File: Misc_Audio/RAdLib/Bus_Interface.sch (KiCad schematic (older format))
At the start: 14 parts, among them J1 Raspberry_Pi_2_3, J2 UART_Header, J3 Power_Output_Header, J4 I2C_Header, U101 74AHCT04, U201 74LVC245A, U202 74HCT245, U203 74AHCT125, U204 M24C01-FDW

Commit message: Checkpoint ... board is close to being done.  Still need to tweak the ground plane.
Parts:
- removed JP1: Jumper_3_Bridged12, Connector_PinHeader_2.54mm:PinHeader_1x03_P2.54mm_Vertical, symbol Jumper:Jumper_3_Bridged12
- added C201, C202, C203, C204: .1uF, Capacitor_THT:C_Disc_D5.0mm_W2.5mm_P2.50mm, symbol Device:C_Small
- added JP1: Jumper_2_Open, Connector_PinHeader_2.54mm:PinHeader_1x02_P2.54mm_Vertical, symbol Jumper:Jumper_2_Open
- added R205: 1K, Resistor_THT:R_Axial_DIN0204_L3.6mm_D1.6mm_P5.08mm_Horizontal, symbol Device:R
- J2, J3: footprint Connector_PinHeader_2.54mm:PinHeader_1x03_P2.54mm_Horizontal -> Connector_PinHeader_2.54mm:PinHeader_1x03_P2.54mm_Vertical
- J4: footprint Connector_PinHeader_2.54mm:PinHeader_1x02_P2.54mm_Horizontal -> Connector_PinHeader_2.54mm:PinHeader_1x02_P2.54mm_Vertical
- U203: footprint Package_DIP:DIP-20_W7.62mm -> Package_DIP:DIP-14_W7.62mm
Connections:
- wire segments 75 -> 77

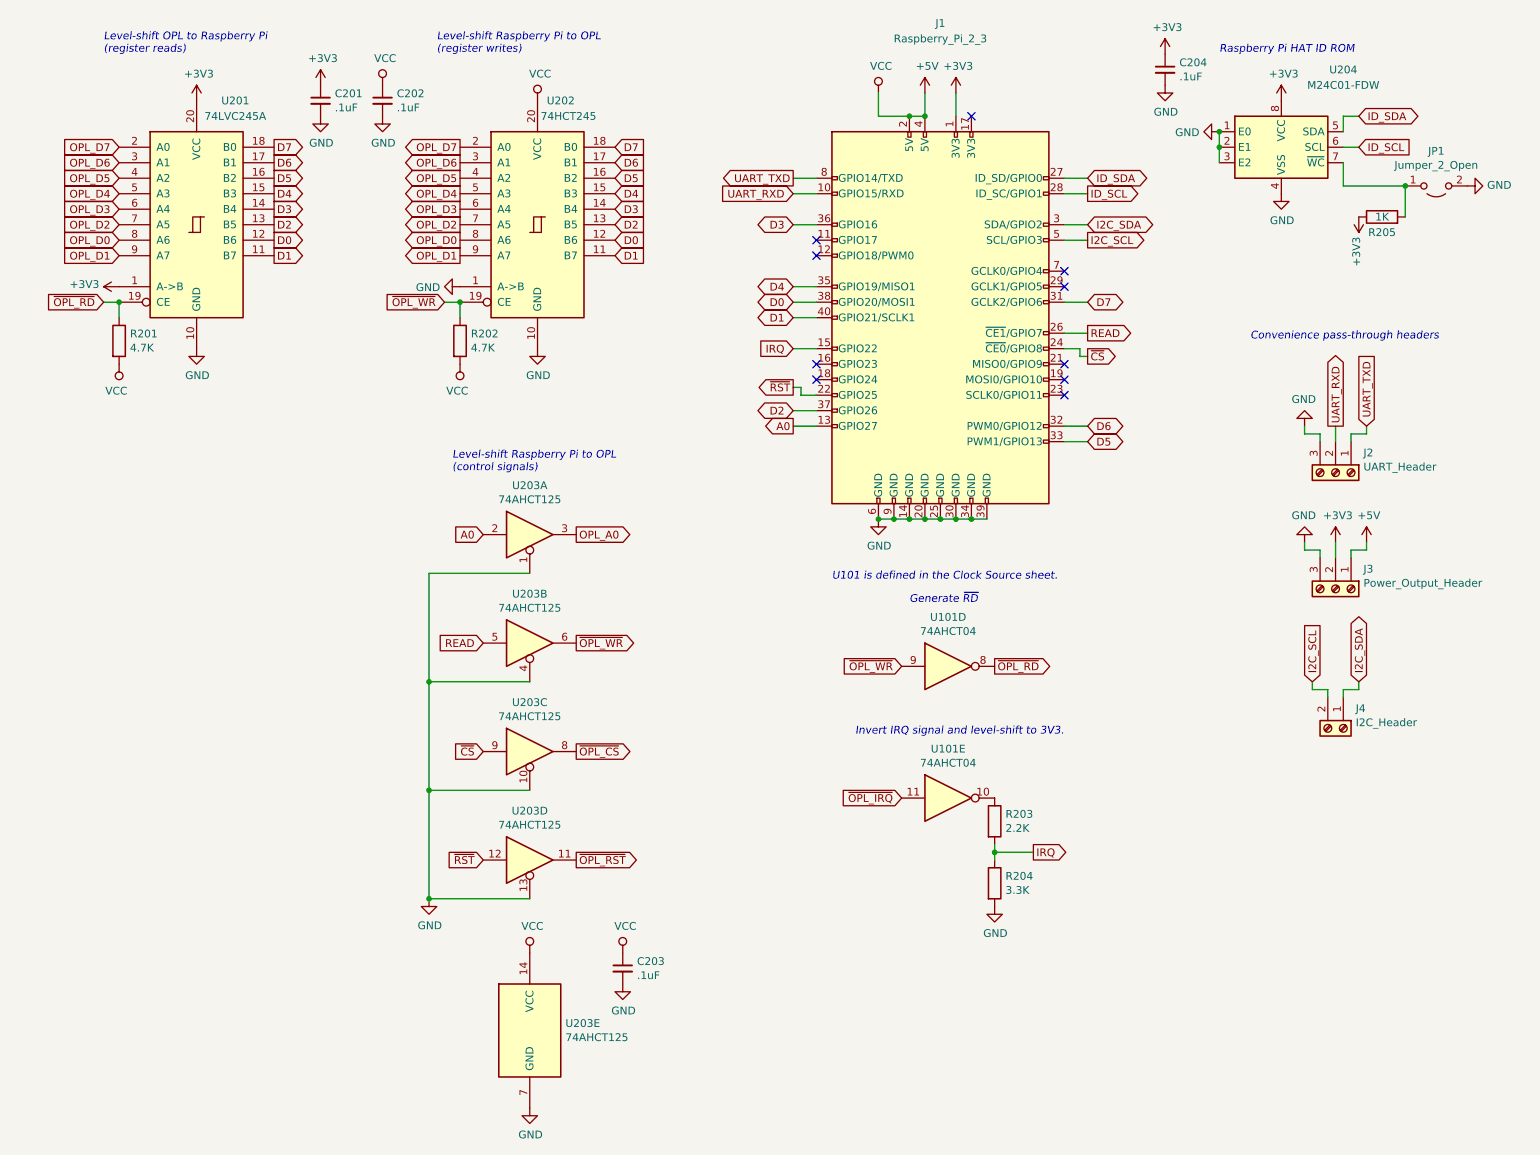
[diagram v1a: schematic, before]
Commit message: Rework the clock to use a self-contained oscillator package.  Remove dependencies on the 7404 in the bus interface.
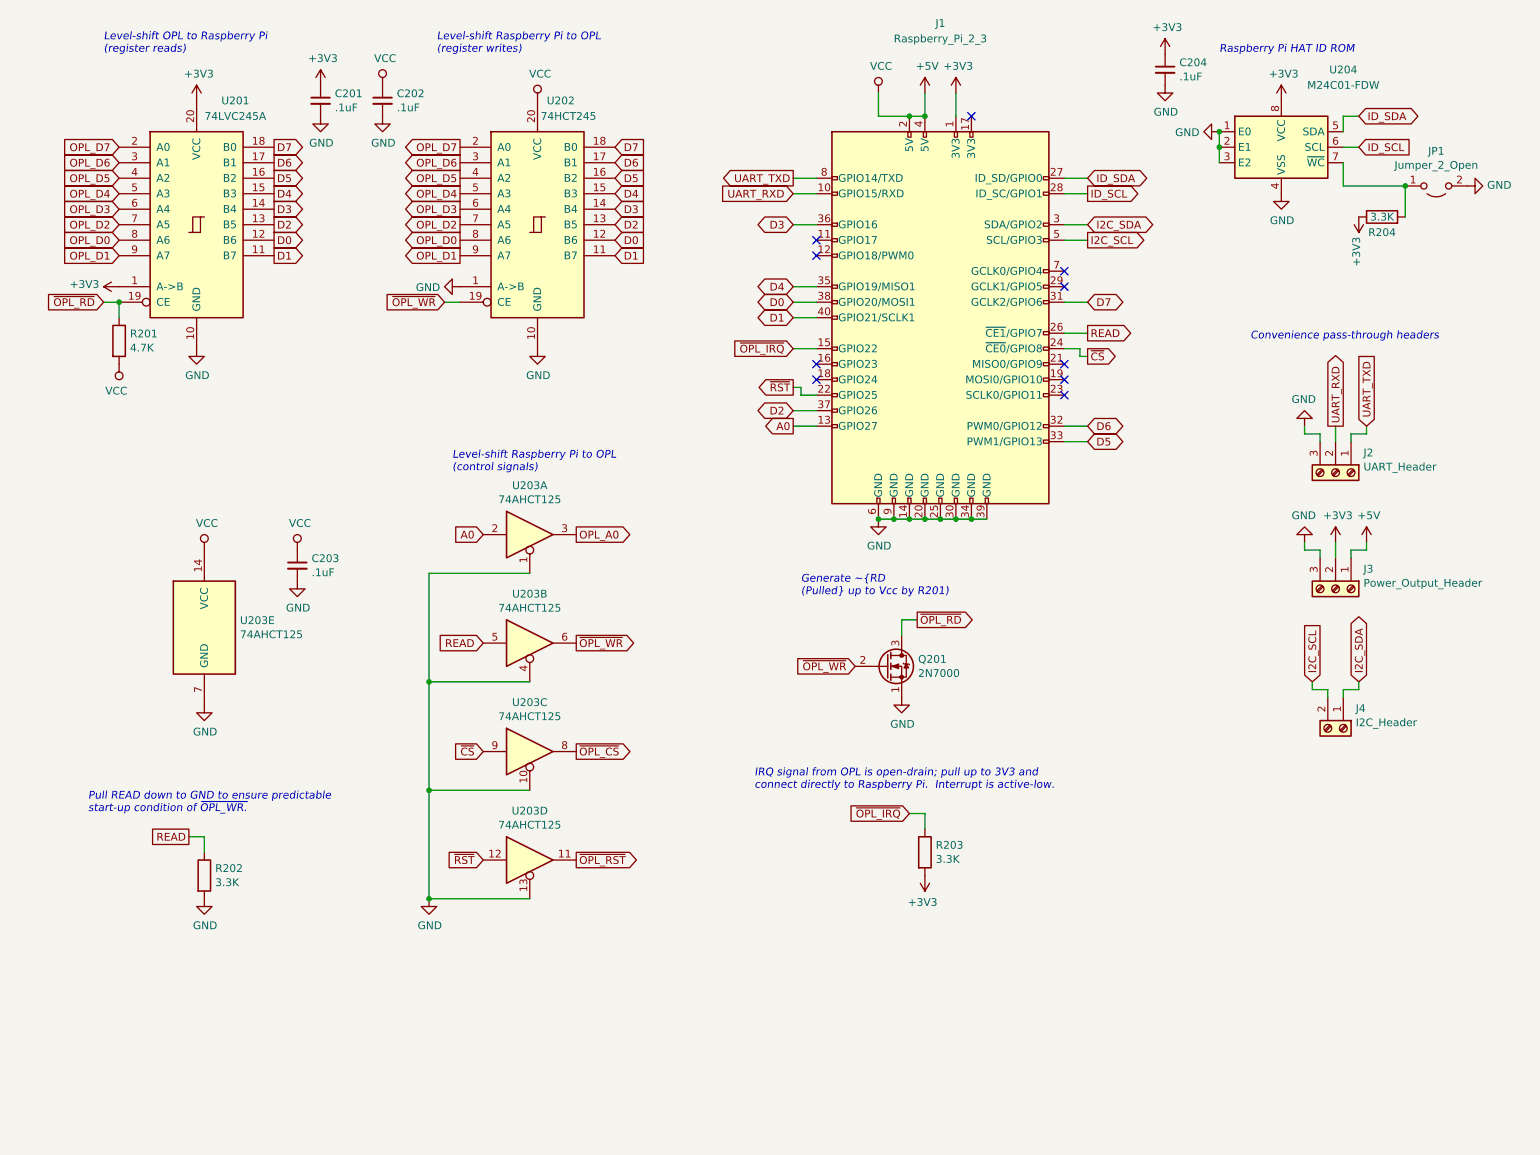
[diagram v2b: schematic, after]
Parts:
- removed R204: 3.3K, Resistor_THT:R_Axial_DIN0204_L3.6mm_D1.6mm_P5.08mm_Horizontal, symbol Device:R
- removed U101: 74AHCT04, Package_DIP:DIP-14_W7.62mm, symbol 74xx:74HC04
- added Q201: 2N7000, Package_TO_SOT_THT:TO-92_HandSolder, symbol Transistor_FET:2N7000
- R202: value 4.7K -> 3.3K; Part Xicon 270-4.7K/REEL-RC -> Xicon 270-3.3K/REEL-RC
- R203: value 2.2K -> 3.3K; Part Xicon 270-2.2K/REEL-RC -> Xicon 270-3.3K/REEL-RC
- R204: renamed from R205; value 1K -> 3.3K
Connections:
- net +3V3: now also R203.2
- net +5V: no longer R202.2
- net GND: now also R202.2, Q201.1 (S)
- net READ: now also R202.1
- net ~OPL_IRQ: now also J1.15 (GPIO22), R203.1
- net ~OPL_RD: now also Q201.3 (D)
- net ~OPL_WR: now also Q201.2 (G); no longer R202.1
- removed net IRQ: J1.15 (GPIO22), R203.2
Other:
- note added: "Generate ~RD\n(Pulled up to Vcc by R201)"
- note added: "IRQ signal from OPL is open-drain; pull up to 3V3 and\nconnect directly to Raspberry Pi. Interrupt is active-low."
- note added: "Pull READ down to GND to ensure predictable\nstart-up condition of ~OPL_WR."
- note removed: "Generate ~RD"
- note removed: "Invert IRQ signal and level-shift to 3V3."
- note removed: "U101 is defined in the Clock Source sheet."
- moved on the sheet: C203, R202, R203, U203E
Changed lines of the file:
@@
 $Descr USLetter 11000 8500
 encoding utf-8
-Sheet 3 3
+Sheet 2 2
 Title "RAdLib - AdLib clone for Raspberry Pi"
 Date "2019-10-10"
@@
 Text GLabel 7300 2750 2    50   Output ~ 0
 READ
-$Comp
-L 74xx:74HC04 U101
-U 4 1 5DA5D1AF
-P 6400 4900
-F 0 "U101" H 6400 5217 50  0000 C CNN
-F 1 "74AHCT04" H 6400 5126 50  0000 C CNN
-F 2 "Package_DIP:DIP-14_W7.62mm" H 6400 4900 50  0001 C CNN
-F 3 "https://assets.nexperia.com/documents/data-sheet/74HC_HCT04.pdf" H 6400 4900 50  0001 C CNN
-	4    6400 4900
-	1    0    0    -1
-$EndComp
-Text GLabel 6100 4900 0    50   Input ~ 0
+Text GLabel 5800 4900 0    50   Input ~ 0
 ~OPL_WR
-Text GLabel 6700 4900 2    50   Output ~ 0
+Text GLabel 6200 4600 2    50   Output ~ 0
 ~OPL_RD
 Wire Wire Line
@@
 	7150 2750 7300 2750
 Text GLabel 5400 2850 0    50   Input ~ 0
-IRQ
+~OPL_IRQ
 NoConn ~ 7150 3050
 NoConn ~ 7150 2950
@@
 L Device:R R202
 U 1 1 5DCAA178
-P 3250 2800
-F 0 "R202" H 3320 2846 50  0000 L CNN
-F 1 "4.7K" H 3320 2755 50  0000 L CNN
-F 2 "Resistor_THT:R_Axial_DIN0204_L3.6mm_D1.6mm_P5.08mm_Horizontal" V 3180 2800 50  0001 C CNN
-F 3 "~" H 3250 2800 50  0001 C CNN
-F 4 "Xicon 270-4.7K/REEL-RC" H 3250 2800 50  0001 C CNN "Part"
-	1    3250 2800
+P 1600 6250
+F 0 "R202" H 1670 6296 50  0000 L CNN
+F 1 "3.3K" H 1670 6205 50  0000 L CNN
+F 2 "Resistor_THT:R_Axial_DIN0204_L3.6mm_D1.6mm_P5.08mm_Horizontal" V 1530 6250 50  0001 C CNN
+F 3 "~" H 1600 6250 50  0001 C CNN
+F 4 "Xicon 270-3.3K/REEL-RC" H 1600 6250 50  0001 C CNN "Part"
+	1    1600 6250
 	1    0    0    -1
 $EndComp
@@
 Wire Wire Line
 	3150 2550 3250 2550
-Wire Wire Line
-	3250 2650 3250 2550
-Connection ~ 3250 2550
-$Comp
-L power:VCC #PWR0135
-U 1 1 5DCB12D8
-P 3250 2950
-F 0 "#PWR0135" H 3250 2800 50  0001 C CNN
-F 1 "VCC" H 3268 3123 50  0000 C CNN
-F 2 "" H 3250 2950 50  0001 C CNN
-F 3 "" H 3250 2950 50  0001 C CNN
-	1    3250 2950
-	-1   0    0    1
-$EndComp
 $Comp
 L 74xx:74LS125 U203
 U 5 1 5DCCCFE6
-P 3700 7250
-F 0 "U203" H 3930 7296 50  0000 L CNN
-F 1 "74AHCT125" H 3930 7205 50  0000 L CNN
-F 2 "Package_DIP:DIP-14_W7.62mm" H 3700 7250 50  0001 C CNN
-F 3 "http://www.ti.com/lit/gpn/sn74LS125" H 3700 7250 50  0001 C CNN
-	5    3700 7250
+P 1600 4650
+F 0 "U203" H 1830 4696 50  0000 L CNN
+F 1 "74AHCT125" H 1830 4605 50  0000 L CNN
+F 2 "Package_DIP:DIP-14_W7.62mm" H 1600 4650 50  0001 C CNN
+F 3 "http://www.ti.com/lit/gpn/sn74LS125" H 1600 4650 50  0001 C CNN
+	5    1600 4650
 	1    0    0    -1
 $EndComp
@@
 L power:VCC #PWR0136
 U 1 1 5DCD0443
-P 3700 6750
-F 0 "#PWR0136" H 3700 6600 50  0001 C CNN
-F 1 "VCC" H 3717 6923 50  0000 C CNN
-F 2 "" H 3700 6750 50  0001 C CNN
-F 3 "" H 3700 6750 50  0001 C CNN
-	1    3700 6750
+P 1600 4150
+F 0 "#PWR0136" H 1600 4000 50  0001 C CNN
+F 1 "VCC" H 1617 4323 50  0000 C CNN
+F 2 "" H 1600 4150 50  0001 C CNN
+F 3 "" H 1600 4150 50  0001 C CNN
+	1    1600 4150
 	1    0    0    -1
 $EndComp
@@
 L power:GND #PWR0137
 U 1 1 5DCD09A2
-P 3700 7750
-F 0 "#PWR0137" H 3700 7500 50  0001 C CNN
-F 1 "GND" H 3705 7577 50  0000 C CNN
-F 2 "" H 3700 7750 50  0001 C CNN
-F 3 "" H 3700 7750 50  0001 C CNN
-	1    3700 7750
+P 1600 5150
+F 0 "#PWR0137" H 1600 4900 50  0001 C CNN
+F 1 "GND" H 1605 4977 50  0000 C CNN
+F 2 "" H 1600 5150 50  0001 C CNN
+F 3 "" H 1600 5150 50  0001 C CNN
+	1    1600 5150
 	1    0    0    -1
 $EndComp
@@
 $EndComp
 Connection ~ 3050 6400
-Text GLabel 6100 5750 0    50   Input ~ 0
+Text GLabel 6150 5850 0    50   Input ~ 0
 ~OPL_IRQ
-$Comp
-L 74xx:74HC04 U101
-U 5 1 5DCDD39D
-P 6400 5750
-F 0 "U101" H 6400 6067 50  0000 C CNN
-F 1 "74AHCT04" H 6400 5976 50  0000 C CNN
-F 2 "Package_DIP:DIP-14_W7.62mm" H 6400 5750 50  0001 C CNN
-F 3 "https://assets.nexperia.com/documents/data-sheet/74HC_HCT04.pdf" H 6400 5750 50  0001 C CNN
-	5    6400 5750
-	1    0    0    -1
-$EndComp
 $Comp
 L Device:R R203
 U 1 1 5DCDEB3B
-P 6700 5900
-F 0 "R203" H 6770 5946 50  0000 L CNN
-F 1 "2.2K" H 6770 5855 50  0000 L CNN
-F 2 "Resistor_THT:R_Axial_DIN0204_L3.6mm_D1.6mm_P5.08mm_Horizontal" V 6630 5900 50  0001 C CNN
-F 3 "~" H 6700 5900 50  0001 C CNN
-F 4 "Xicon 270-2.2K/REEL-RC" H 6700 5900 50  0001 C CNN "Part"
-	1    6700 5900
-	1    0    0    -1
-$EndComp
-$Comp
-L Device:R R204
-U 1 1 5DCDF804
-P 6700 6300
-F 0 "R204" H 6770 6346 50  0000 L CNN
-F 1 "3.3K" H 6770 6255 50  0000 L CNN
-F 2 "Resistor_THT:R_Axial_DIN0204_L3.6mm_D1.6mm_P5.08mm_Horizontal" V 6630 6300 50  0001 C CNN
-F 3 "~" H 6700 6300 50  0001 C CNN
-F 4 "Xicon 270-3.3K-RC" H 6700 6300 50  0001 C CNN "Part"
-	1    6700 6300
-	1    0    0    -1
-$EndComp
-$Comp
-L power:GND #PWR0139
-U 1 1 5DCE303F
-P 6700 6450
-F 0 "#PWR0139" H 6700 6200 50  0001 C CNN
-F 1 "GND" H 6705 6277 50  0000 C CNN
-F 2 "" H 6700 6450 50  0001 C CNN
-F 3 "" H 6700 6450 50  0001 C CNN
-	1    6700 6450
-	1    0    0    -1
-$EndComp
-Wire Wire Line
-	6700 6050 6700 6100
-Text GLabel 6950 6100 2    50   Output ~ 0
-IRQ
-Wire Wire Line
-	6700 6100 6950 6100
-Connection ~ 6700 6100
-Wire Wire Line
-	6700 6100 6700 6150
-Text Notes 5800 5350 0    50   Italic 0
-Invert IRQ signal and level-shift to 3V3.
+P 6250 6100
+F 0 "R203" H 6320 6146 50  0000 L CNN
+F 1 "3.3K" H 6320 6055 50  0000 L CNN
+F 2 "Resistor_THT:R_Axial_DIN0204_L3.6mm_D1.6mm_P5.08mm_Horizontal" V 6180 6100 50  0001 C CNN
+F 3 "~" H 6250 6100 50  0001 C CNN
+F 4 "Xicon 270-3.3K/REEL-RC" H 6250 6100 50  0001 C CNN "Part"
+	1    6250 6100
+	1    0    0    -1
+$EndComp
 Text Notes 3200 3650 0    50   Italic 0
 Level-shift Raspberry Pi to OPL\n(control signals)
-Text Notes 6150 4500 0    50   Italic 0
-Generate ~RD
+Text Notes 5450 4450 0    50   Italic 0
+Generate ~RD\n(Pulled up to Vcc by R201)
 Text Notes 8150 950  0    50   Italic 0
 Raspberry Pi HAT ID ROM
 Text Notes 8350 2800 0    50   Italic 0
 Convenience pass-through headers
-Text Notes 5650 4350 0    50   Italic 0
-U101 is defined in the Clock Source sheet.
 NoConn ~ 5550 2150
 Wire Wire Line
@@
 L Device:C_Small C203
 U 1 1 5DA58D30
-P 4300 6850
-F 0 "C203" H 4392 6896 50  0000 L CNN
-F 1 ".1uF" H 4392 6805 50  0000 L CNN
-F 2 "Capacitor_THT:C_Disc_D5.0mm_W2.5mm_P2.50mm" H 4300 6850 50  0001 C CNN
-F 3 "~" H 4300 6850 50  0001 C CNN
-	1    4300 6850
+P 2200 4250
+F 0 "C203" H 2292 4296 50  0000 L CNN
+F 1 ".1uF" H 2292 4205 50  0000 L CNN
+F 2 "Capacitor_THT:C_Disc_D5.0mm_W2.5mm_P2.50mm" H 2200 4250 50  0001 C CNN
+F 3 "~" H 2200 4250 50  0001 C CNN
+	1    2200 4250
 	1    0    0    -1
 $EndComp
@@
 L power:GND #PWR0152
 U 1 1 5DA6179C
-P 4300 6950
-F 0 "#PWR0152" H 4300 6700 50  0001 C CNN
-F 1 "GND" H 4305 6777 50  0000 C CNN
-F 2 "" H 4300 6950 50  0001 C CNN
-F 3 "" H 4300 6950 50  0001 C CNN
-	1    4300 6950
+P 2200 4350
+F 0 "#PWR0152" H 2200 4100 50  0001 C CNN
+F 1 "GND" H 2205 4177 50  0000 C CNN
+F 2 "" H 2200 4350 50  0001 C CNN
+F 3 "" H 2200 4350 50  0001 C CNN
+	1    2200 4350
 	1    0    0    -1
 $EndComp
@@
 L power:VCC #PWR0153
 U 1 1 5DA61DAB
-P 4300 6750
-F 0 "#PWR0153" H 4300 6600 50  0001 C CNN
-F 1 "VCC" H 4317 6923 50  0000 C CNN
-F 2 "" H 4300 6750 50  0001 C CNN
-F 3 "" H 4300 6750 50  0001 C CNN
-	1    4300 6750
+P 2200 4150
+F 0 "#PWR0153" H 2200 4000 50  0001 C CNN
+F 1 "VCC" H 2217 4323 50  0000 C CNN
+F 2 "" H 2200 4150 50  0001 C CNN
+F 3 "" H 2200 4150 50  0001 C CNN
+	1    2200 4150
 	1    0    0    -1
 $EndComp
@@
 $EndComp
 $Comp
-L Device:R R205
+L Device:R R204
 U 1 1 5DBFD35A
 P 9200 2000
-F 0 "R205" V 9100 2000 50  0000 C CNN
-F 1 "1K" V 9200 2000 50  0000 C CNN
+F 0 "R204" V 9100 2000 50  0000 C CNN
+F 1 "3.3K" V 9200 2000 50  0000 C CNN
 F 2 "Resistor_THT:R_Axial_DIN0204_L3.6mm_D1.6mm_P5.08mm_Horizontal" V 9130 2000 50  0001 C CNN
 F 3 "~" H 9200 2000 50  0001 C CNN
@@
 	9350 1800 9350 2000
 Connection ~ 9350 1800
+$Comp
+L power:GND #PWR0135
+U 1 1 5DB0A057
+P 6100 5100
+F 0 "#PWR0135" H 6100 4850 50  0001 C CNN
+F 1 "GND" H 6105 4927 50  0000 C CNN
+F 2 "" H 6100 5100 50  0001 C CNN
+F 3 "" H 6100 5100 50  0001 C CNN
+	1    6100 5100
+	1    0    0    -1
+$EndComp
+Wire Wire Line
+	6100 4700 6100 4600
+Wire Wire Line
+	6100 4600 6200 4600
+$Comp
+L Transistor_FET:2N7000 Q201
+U 1 1 5DB155F3
+P 6000 4900
+F 0 "Q201" H 6206 4946 50  0000 L CNN
+F 1 "2N7000" H 6206 4855 50  0000 L CNN
+F 2 "Package_TO_SOT_THT:TO-92_HandSolder" H 6200 4825 50  0001 L CIN
+F 3 "https://www.fairchildsemi.com/datasheets/2N/2N7000.pdf" H 6000 4900 50  0001 L CNN
+	1    6000 4900
+	1    0    0    -1
+$EndComp
+Text Notes 5150 5700 0    50   Italic 0
+IRQ signal from OPL is open-drain; pull up to 3V3 and\nconnect directly to Raspberry Pi.  Interrupt is active-low.
+$Comp
+L power:+3V3 #PWR0139
+U 1 1 5DB18514
+P 6250 6250
+F 0 "#PWR0139" H 6250 6100 50  0001 C CNN
+F 1 "+3V3" H 6265 6423 50  0000 C CNN
+F 2 "" H 6250 6250 50  0001 C CNN
+F 3 "" H 6250 6250 50  0001 C CNN
+	1    6250 6250
+	-1   0    0    1
+$EndComp
+Wire Wire Line
+	6150 5850 6250 5850
+Wire Wire Line
+	6250 5850 6250 5950
+$Comp
+L power:GND #PWR0146
+U 1 1 5DB32E2F
+P 1600 6400
+F 0 "#PWR0146" H 1600 6150 50  0001 C CNN
+F 1 "GND" H 1605 6227 50  0000 C CNN
+F 2 "" H 1600 6400 50  0001 C CNN
+F 3 "" H 1600 6400 50  0001 C CNN
+	1    1600 6400
+	1    0    0    -1
+$EndComp
+Text GLabel 1500 6000 0    50   UnSpc ~ 0
+READ
+Wire Wire Line
+	1500 6000 1600 6000
+Wire Wire Line
+	1600 6000 1600 6100
+Text Notes 850  5850 0    50   Italic 0
+Pull READ down to GND to ensure predictable\nstart-up condition of ~OPL_WR.
 $EndSCHEMATC
